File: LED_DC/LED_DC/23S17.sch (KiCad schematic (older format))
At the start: 27 parts

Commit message: Removed redundant files
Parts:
- removed C?: CP, symbol Device:CP
- removed R? (x9): 10K, symbol Device:R
- removed U?: MCP23S17_SO, Package_SO:SOIC-28W_7.5x17.9mm_P1.27mm, symbol Interface_Expansion:MCP23S17_SO
- added DS?: HY1602E, Display:HY1602E, symbol Display_Character:HY1602E
- added R10, R11, R4, R5, R6, R7, R8, R9: R, symbol Device:R
- added U1: 74HC238, symbol 74xx_IEEE:74HC238
- added U2: ULN2803A, symbol Transistor_Array:ULN2803A
- gave numbers to parts that had none: 16
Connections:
- net labels added: +5V, I1, I2, I3, I_A, I_B, I_C, I_D, I_DP, I_E, I_F, I_G
- net labels removed: MISO, MOSI, SCLK, SS
- wire segments 39 -> 56
- no-connect marks 0 -> 1
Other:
- note added: "COMM is generally used during driving Relays, for LEDs not needed"
- note added: "Digit Chose X"
- note added: "Digit Scan selection Decoder logic"
- note added: "Future Support For LCD Display."
- note added: "High Side,"
- note added: "Low Side, LED Segment Current Sink Driver"
- note added: "Segment Chose X"
- moved on the sheet: R12, R13, R14, R15, R16, R17, R18, R19

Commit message: updated the led schematic.
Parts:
- removed Q2, Q3, Q4, Q5, Q6, Q7, Q8: FDV304P, digikey-footprints:SOT-23-3, symbol dk_Transistors-FETs-MOSFETs-Single:DMG2305UX-13
- removed R12, R16: R, symbol Device:R
- removed R13, R14, R15, R17, R18, R19: 10K, symbol Device:R
- added Q? (x7): FDV304P, digikey-footprints:SOT-23-3, symbol LED_DC-rescue:DMG2305UX-13-dk_Transistors-FETs-MOSFETs-Single
- Q1: symbol dk_Transistors-FETs-MOSFETs-Single:DMG2305UX-13 -> LED_DC-rescue:DMG2305UX-13-dk_Transistors-FETs-MOSFETs-Single
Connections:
- net labels added: C1, C2, C3, D0, D1, D2, D3, D4, D5, D6, D7
- wire segments 56 -> 73
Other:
- moved on the sheet: DS?, R5

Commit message: Added keypad connector.
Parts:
- removed R10, R11, R5, R6, R7, R8, R9: R, symbol Device:R
- added R? (x7): R, symbol Device:R
- added R? (x3): R_Small, symbol Device:R_Small
- added TP?: TestPoint, symbol Connector:TestPoint
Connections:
- net labels removed: +3.3V, I1, I2, I3, I_A, I_B, I_C, I_D, I_DP, I_E, I_F, I_G, VDD
- wire segments 73 -> 74
- no-connect marks 1 -> 0
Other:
- moved on the sheet: R4

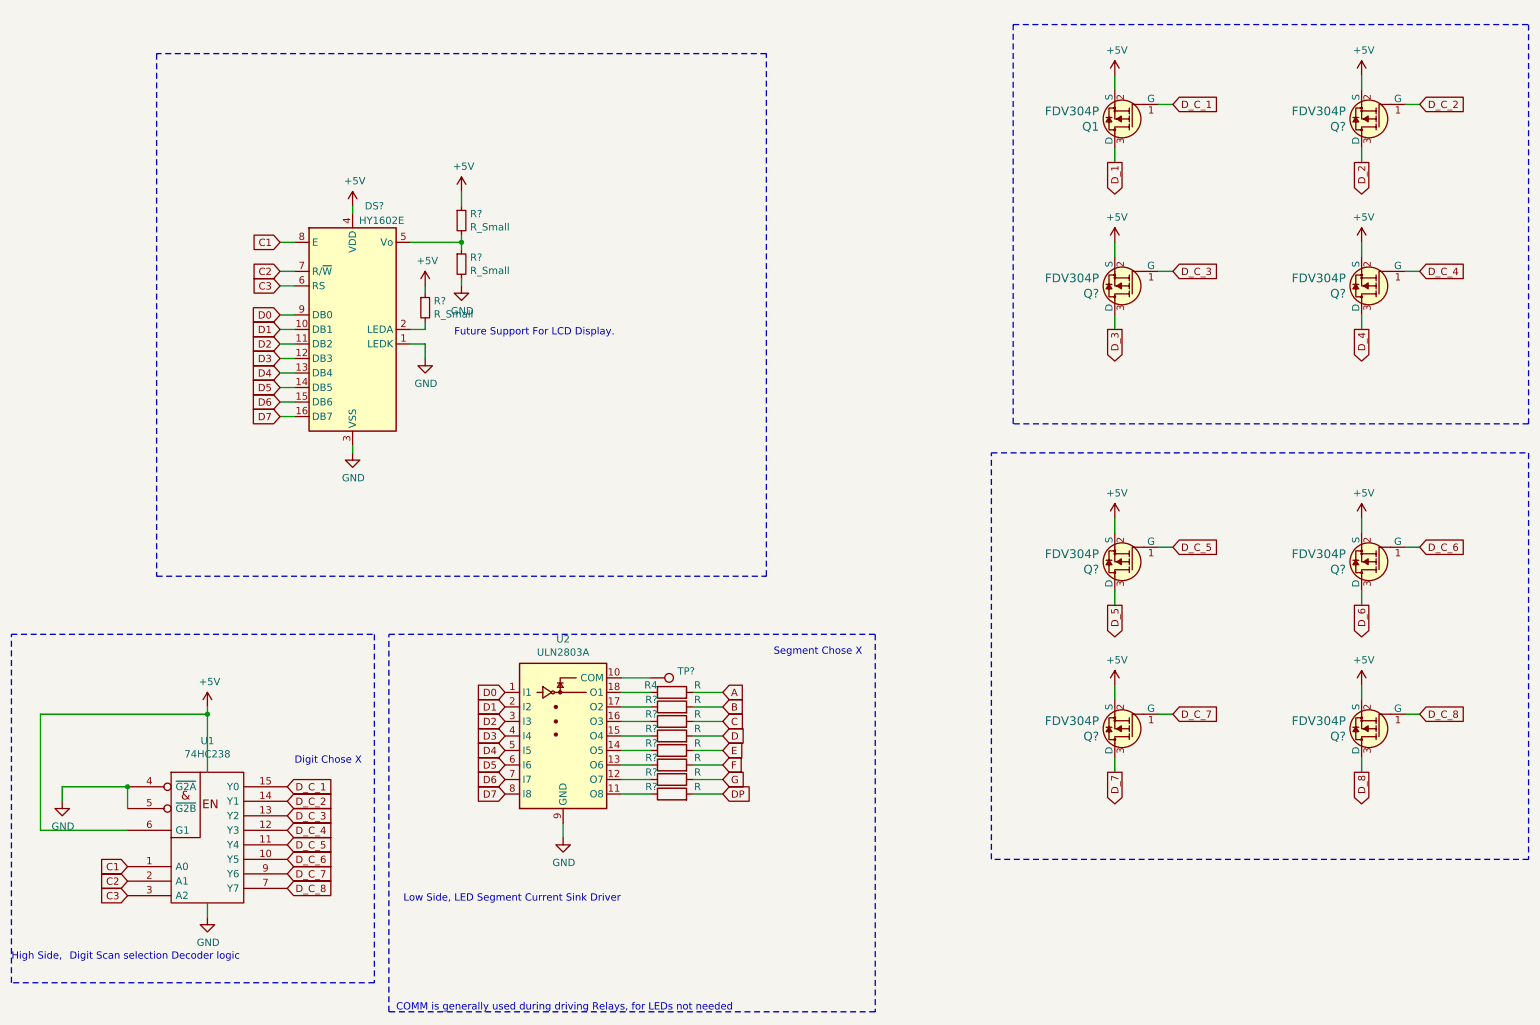
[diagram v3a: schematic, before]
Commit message: Added foot prints for the components.
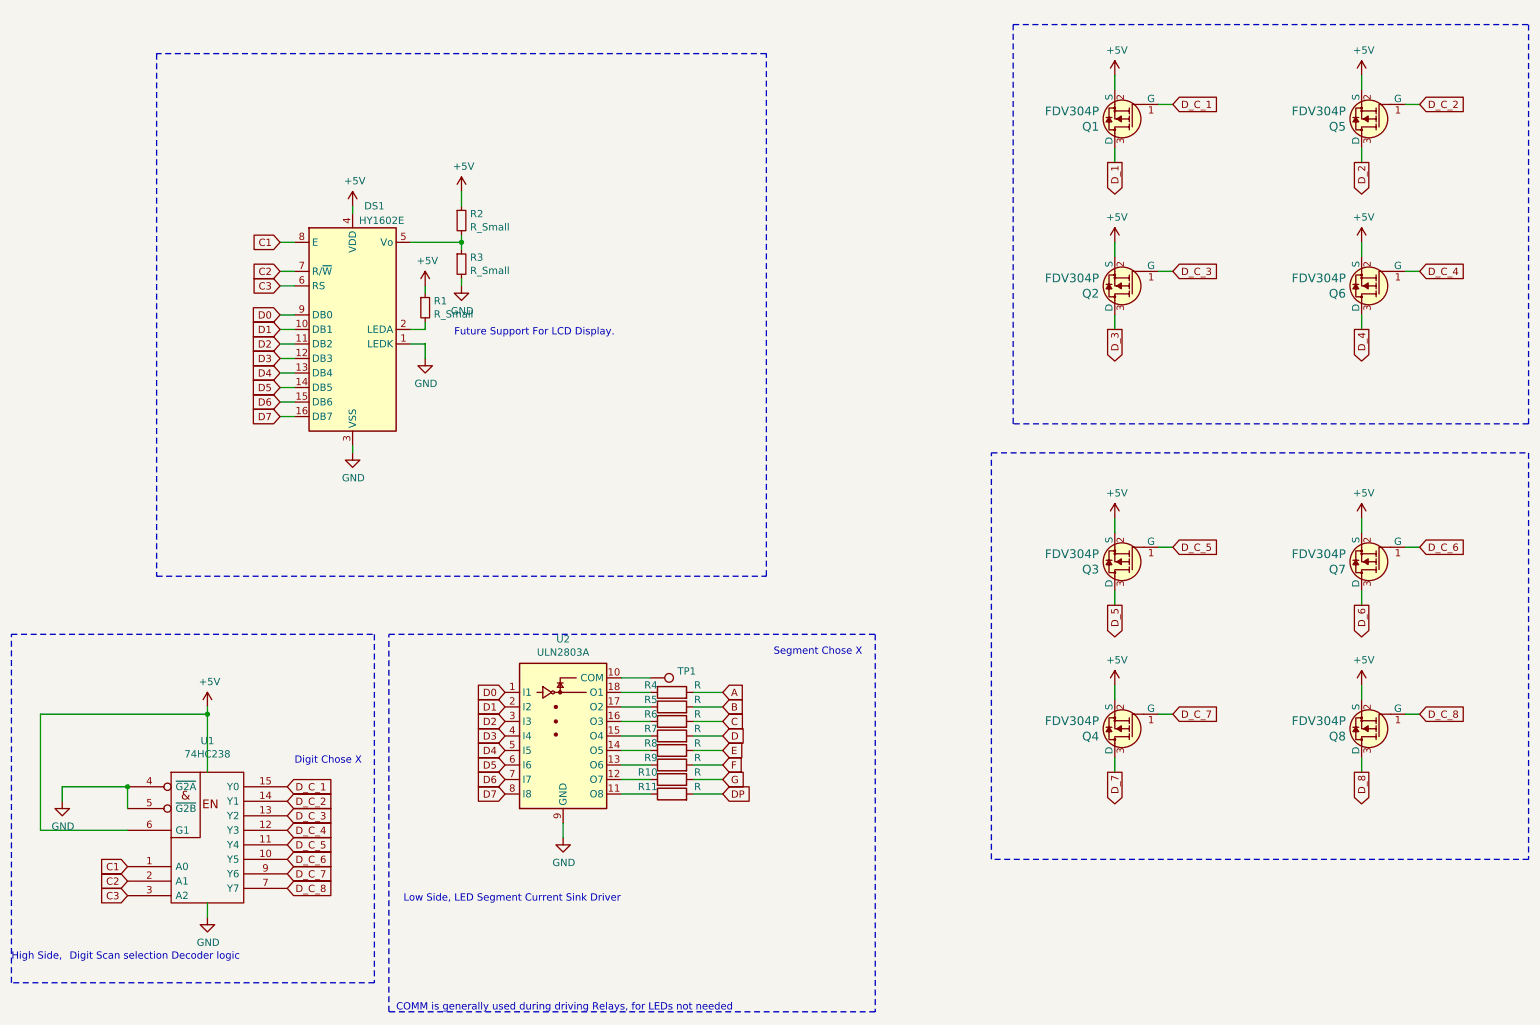
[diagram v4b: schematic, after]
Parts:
- Q1: footprint digikey-footprints:SOT-23-3 -> Package_TO_SOT_SMD:SOT-23_Handsoldering
- Q2, Q3, Q4, Q5, Q6, Q7, Q8: renamed from Q?; footprint digikey-footprints:SOT-23-3 -> Package_TO_SOT_SMD:SOT-23_Handsoldering
- R1, R10, R11, R2, R3, R5, R6, R7, R8, R9: renamed from R?; footprint (none) -> Resistor_SMD:R_0603_1608Metric
- R4: footprint (none) -> Resistor_SMD:R_0603_1608Metric
- TP1: renamed from TP?; footprint (none) -> TestPoint:TestPoint_Pad_D1.5mm
- U1: footprint (none) -> Package_SO:SO-16_3.9x9.9mm_P1.27mm
- U2: footprint (none) -> Package_SO:SOIC-18W_7.5x11.6mm_P1.27mm
- gave numbers to parts that had none: 1

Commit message: updated the PCB.
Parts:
- DS1: footprint Display:HY1602E -> Connector_PinHeader_2.54mm:PinHeader_1x16_P2.54mm_Vertical
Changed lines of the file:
@@
 F 0 "DS1" H 3000 3550 50  0000 C CNN
 F 1 "HY1602E" H 3050 3450 50  0000 C CNN
-F 2 "Display:HY1602E" H 2850 1800 50  0001 C CIN
+F 2 "Connector_PinHeader_2.54mm:PinHeader_1x16_P2.54mm_Vertical" H 2850 1800 50  0001 C CIN
 F 3 "http://www.icbank.com/data/ICBShop/board/HY1602E.pdf" H 3050 2800 50  0001 C CNN
 	1    2850 2700

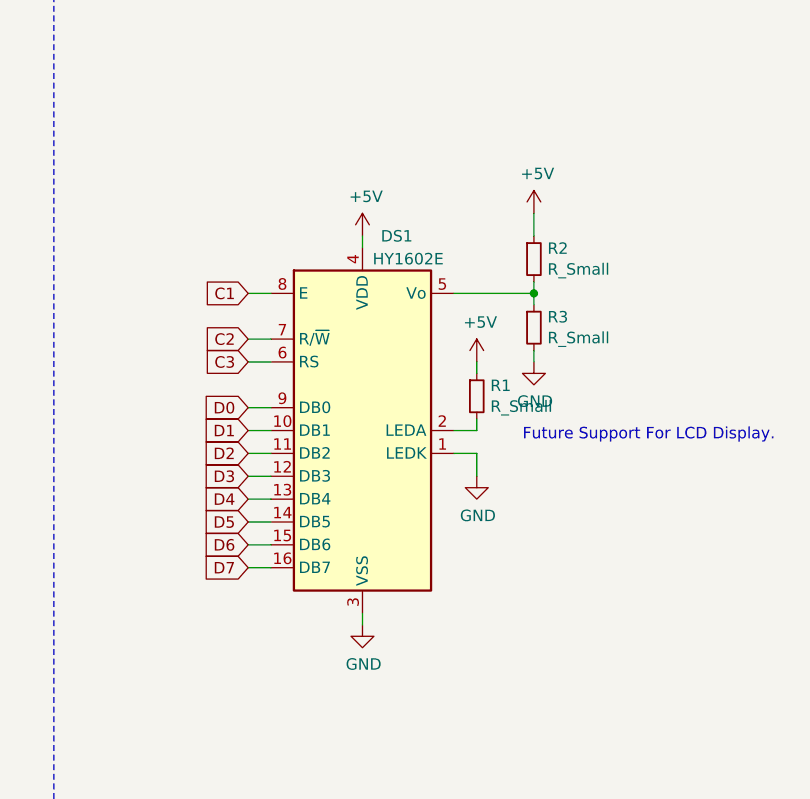
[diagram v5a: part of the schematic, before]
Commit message: updated the schematic after feedback.
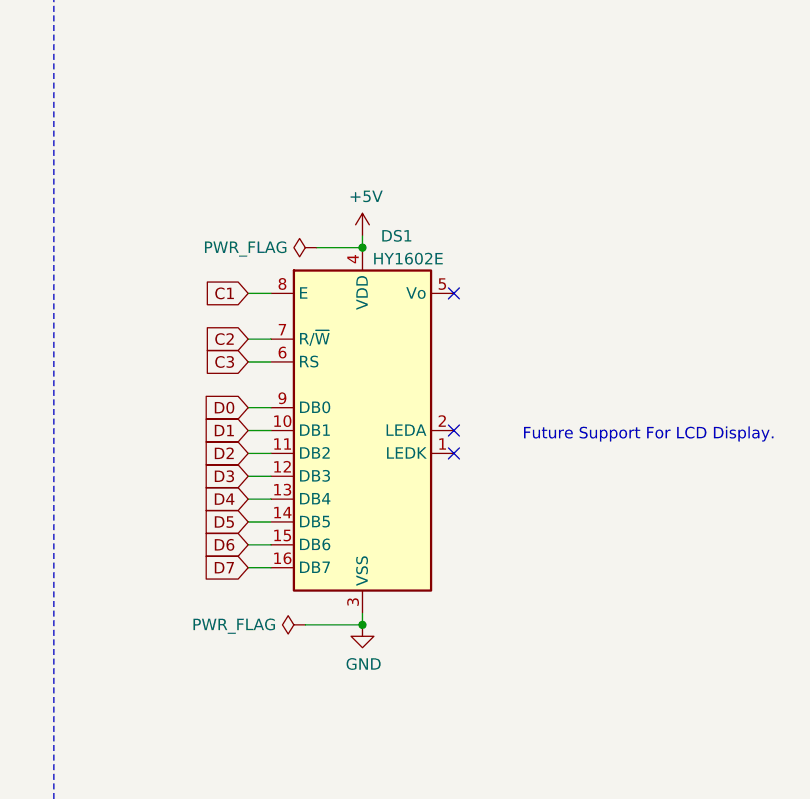
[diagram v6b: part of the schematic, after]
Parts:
- removed R1, R2, R3: R_Small, Resistor_SMD:R_0603_1608Metric, symbol Device:R_Small
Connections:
- net GND: no longer DS1.1 (LEDK)
- no-connect marks 0 -> 3
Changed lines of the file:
@@
 COMM is generally used during driving Relays, for LEDs not needed
-$Comp
-L Display_Character:HY1602E DS1
-U 1 1 5FC030D8
-P 2850 2700
-F 0 "DS1" H 3000 3550 50  0000 C CNN
-F 1 "HY1602E" H 3050 3450 50  0000 C CNN
-F 2 "Connector_PinHeader_2.54mm:PinHeader_1x16_P2.54mm_Vertical" H 2850 1800 50  0001 C CIN
-F 3 "http://www.icbank.com/data/ICBShop/board/HY1602E.pdf" H 3050 2800 50  0001 C CNN
-	1    2850 2700
-	1    0    0    -1
-$EndComp
 $Comp
 L power:+5V #PWR05
@@
 Wire Notes Line
 	5700 800  1500 800
-Text Notes 3550 2750 0    50   ~ 0
-Future Support For LCD Display.
 Wire Wire Line
 	2850 3500 2850 3550
@@
 	4900 5100 4700 5100
 $Comp
-L power:GND #PWR010
-U 1 1 5FEAB2F7
-P 3350 2900
-F 0 "#PWR010" H 3350 2650 50  0001 C CNN
-F 1 "GND" H 3355 2727 50  0000 C CNN
-F 2 "" H 3350 2900 50  0001 C CNN
-F 3 "" H 3350 2900 50  0001 C CNN
-	1    3350 2900
-	1    0    0    -1
-$EndComp
-$Comp
-L power:+5V #PWR09
-U 1 1 5FEAB829
-P 3350 2400
-F 0 "#PWR09" H 3350 2250 50  0001 C CNN
-F 1 "+5V" H 3365 2573 50  0000 C CNN
-F 2 "" H 3350 2400 50  0001 C CNN
-F 3 "" H 3350 2400 50  0001 C CNN
-	1    3350 2400
-	1    0    0    -1
-$EndComp
-$Comp
-L Device:R_Small R1
-U 1 1 5FEAC3CE
-P 3350 2550
-F 0 "R1" H 3409 2596 50  0000 L CNN
-F 1 "R_Small" H 3409 2505 50  0000 L CNN
-F 2 "Resistor_SMD:R_0603_1608Metric" H 3350 2550 50  0001 C CNN
-F 3 "~" H 3350 2550 50  0001 C CNN
-	1    3350 2550
-	1    0    0    -1
-$EndComp
-Wire Wire Line
-	3350 2650 3350 2700
-Wire Wire Line
-	3350 2700 3250 2700
-Wire Wire Line
-	3250 2800 3350 2800
-Wire Wire Line
-	3350 2800 3350 2900
-Wire Wire Line
-	3350 2450 3350 2400
-$Comp
-L Device:R_Small R2
-U 1 1 5FEB1440
-P 3600 1950
-F 0 "R2" H 3659 1996 50  0000 L CNN
-F 1 "R_Small" H 3659 1905 50  0000 L CNN
-F 2 "Resistor_SMD:R_0603_1608Metric" H 3600 1950 50  0001 C CNN
-F 3 "~" H 3600 1950 50  0001 C CNN
-	1    3600 1950
-	1    0    0    -1
-$EndComp
-$Comp
-L Device:R_Small R3
-U 1 1 5FEB1C82
-P 3600 2250
-F 0 "R3" H 3659 2296 50  0000 L CNN
-F 1 "R_Small" H 3659 2205 50  0000 L CNN
-F 2 "Resistor_SMD:R_0603_1608Metric" H 3600 2250 50  0001 C CNN
-F 3 "~" H 3600 2250 50  0001 C CNN
-	1    3600 2250
-	1    0    0    -1
-$EndComp
-$Comp
-L power:GND #PWR014
-U 1 1 5FEB1F5D
-P 3600 2400
-F 0 "#PWR014" H 3600 2150 50  0001 C CNN
-F 1 "GND" H 3605 2227 50  0000 C CNN
-F 2 "" H 3600 2400 50  0001 C CNN
-F 3 "" H 3600 2400 50  0001 C CNN
-	1    3600 2400
-	1    0    0    -1
-$EndComp
-$Comp
-L power:+5V #PWR013
-U 1 1 5FEB20FA
-P 3600 1750
-F 0 "#PWR013" H 3600 1600 50  0001 C CNN
-F 1 "+5V" H 3615 1923 50  0000 C CNN
-F 2 "" H 3600 1750 50  0001 C CNN
-F 3 "" H 3600 1750 50  0001 C CNN
-	1    3600 1750
-	1    0    0    -1
-$EndComp
-Wire Wire Line
-	3600 1750 3600 1850
-Wire Wire Line
-	3600 2050 3600 2100
-Wire Wire Line
-	3600 2350 3600 2400
-Wire Wire Line
-	3250 2100 3600 2100
-Connection ~ 3600 2100
-Wire Wire Line
-	3600 2100 3600 2150
+L Display_Character:HY1602E DS1
+U 1 1 5FC030D8
+P 2850 2700
+F 0 "DS1" H 3000 3550 50  0000 C CNN
+F 1 "HY1602E" H 3050 3450 50  0000 C CNN
+F 2 "Connector_PinHeader_2.54mm:PinHeader_1x16_P2.54mm_Vertical" H 2850 1800 50  0001 C CIN
+F 3 "http://www.icbank.com/data/ICBShop/board/HY1602E.pdf" H 3050 2800 50  0001 C CNN
+	1    2850 2700
+	1    0    0    -1
+$EndComp
+Text Notes 3550 2750 0    50   ~ 0
+Future Support For LCD Display.
+NoConn ~ 3250 2100
+NoConn ~ 3250 2700
+NoConn ~ 3250 2800
+$Comp
+L power:PWR_FLAG #FLG0101
+U 1 1 60176418
+P 2650 1900
+F 0 "#FLG0101" H 2650 1975 50  0001 C CNN
+F 1 "PWR_FLAG" V 2650 2027 50  0000 L CNN
+F 2 "" H 2650 1900 50  0001 C CNN
+F 3 "~" H 2650 1900 50  0001 C CNN
+	1    2650 1900
+	0    -1   -1   0
+$EndComp
+$Comp
+L power:PWR_FLAG #FLG0102
+U 1 1 60176CCD
+P 2600 3550
+F 0 "#FLG0102" H 2600 3625 50  0001 C CNN
+F 1 "PWR_FLAG" V 2600 3677 50  0000 L CNN
+F 2 "" H 2600 3550 50  0001 C CNN
+F 3 "~" H 2600 3550 50  0001 C CNN
+	1    2600 3550
+	0    -1   -1   0
+$EndComp
+Wire Wire Line
+	2600 3550 2850 3550
+Connection ~ 2850 3550
+Wire Wire Line
+	2650 1900 2850 1900
+Connection ~ 2850 1900
 $EndSCHEMATC

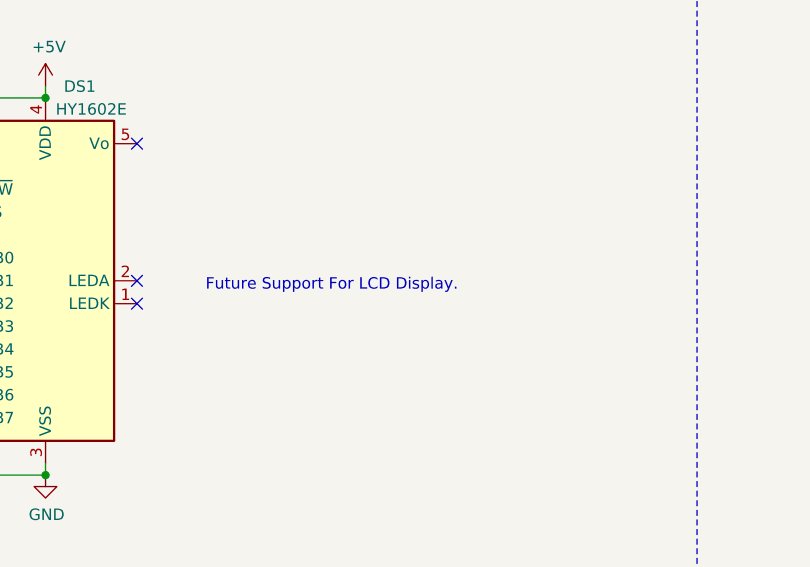
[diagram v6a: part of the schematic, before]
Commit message: Added text to the schematic sections.
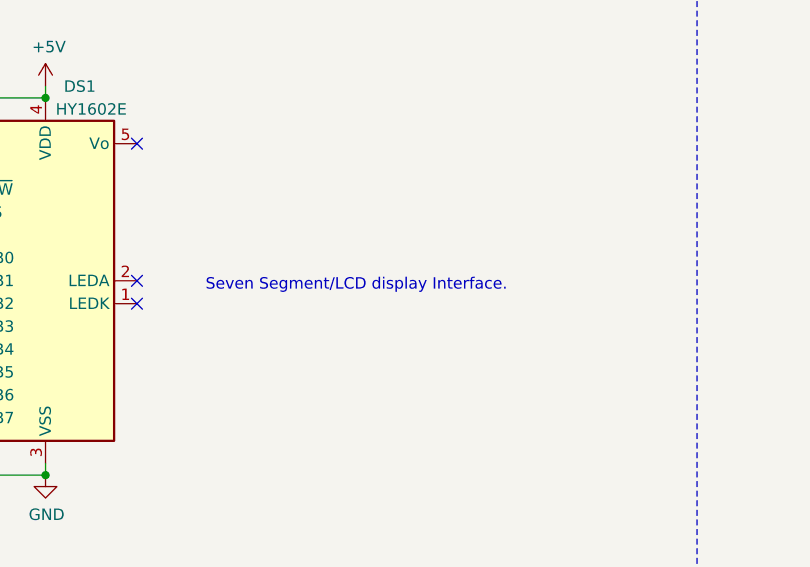
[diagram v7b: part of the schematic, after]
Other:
- note added: "Seven Segment/LCD display Interface."
- note removed: "Future Support For LCD Display."
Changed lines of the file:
@@
 $EndComp
 Text Notes 3550 2750 0    50   ~ 0
-Future Support For LCD Display.
+Seven Segment/LCD display Interface.
 NoConn ~ 3250 2100
 NoConn ~ 3250 2700

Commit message: Updated the schematic.
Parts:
- DS1: value HY1602E -> RC1602A; symbol Display_Character:HY1602E -> Display_Character:RC1602A
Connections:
- net +5V: now also DS1.2 (VDD); no longer DS1.4 (VDD)
- net C1: now also DS1.4 (RS); no longer DS1.8 (E)
- net C2: now also DS1.5 (R/W); no longer DS1.7 (R/~W)
- net D0: now also DS1.7 (DB0); no longer DS1.9 (DB0)
- net D1: now also DS1.8 (DB1); no longer DS1.10 (DB1)
- net D2: now also DS1.9 (DB2); no longer DS1.11 (DB2)
- net D3: now also DS1.10 (DB3); no longer DS1.12 (DB3)
- net D4: now also DS1.11 (DB4); no longer DS1.13 (DB4)
- net D5: now also DS1.12 (DB5); no longer DS1.14 (DB5)
- net D6: now also DS1.13 (DB6); no longer DS1.15 (DB6)
- net D7: now also DS1.14 (DB7); no longer DS1.16 (DB7)
- net GND: now also DS1.1 (VSS); no longer DS1.3 (VSS)
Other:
- moved on the sheet: DS1
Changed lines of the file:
@@
 Wire Wire Line
 	9800 5750 9800 5650
-Text GLabel 2350 2100 0    50   Input ~ 0
+Text GLabel 2350 2300 0    50   Input ~ 0
 C1
-Text GLabel 2350 2300 0    50   Input ~ 0
+Text GLabel 2350 2400 0    50   Input ~ 0
 C2
-Text GLabel 2350 2400 0    50   Input ~ 0
+Text GLabel 2350 2500 0    50   Input ~ 0
 C3
 Text GLabel 2350 2600 0    50   Input ~ 0
@@
 D7
 Wire Wire Line
-	2350 2100 2450 2100
-Wire Wire Line
-	2450 2300 2350 2300
-Wire Wire Line
-	2350 2400 2450 2400
-Wire Wire Line
 	2450 2600 2350 2600
 Wire Wire Line
@@
 	4900 5100 4700 5100
 $Comp
-L Display_Character:HY1602E DS1
+L Display_Character:RC1602A DS1
 U 1 1 5FC030D8
-P 2850 2700
-F 0 "DS1" H 3000 3550 50  0000 C CNN
-F 1 "HY1602E" H 3050 3450 50  0000 C CNN
-F 2 "Connector_PinHeader_2.54mm:PinHeader_1x16_P2.54mm_Vertical" H 2850 1800 50  0001 C CIN
-F 3 "http://www.icbank.com/data/ICBShop/board/HY1602E.pdf" H 3050 2800 50  0001 C CNN
-	1    2850 2700
+P 2850 2800
+F 0 "DS1" H 3000 3650 50  0000 C CNN
+F 1 "RC1602A" H 3050 3550 50  0000 C CNN
+F 2 "Connector_PinHeader_2.54mm:PinHeader_1x16_P2.54mm_Vertical" H 2850 1900 50  0001 C CIN
+F 3 "http://www.icbank.com/data/ICBShop/board/HY1602E.pdf" H 3050 2900 50  0001 C CNN
+	1    2850 2800
 	1    0    0    -1
 $EndComp
 Text Notes 3550 2750 0    50   ~ 0
 Seven Segment/LCD display Interface.
-NoConn ~ 3250 2100
-NoConn ~ 3250 2700
-NoConn ~ 3250 2800
 $Comp
 L power:PWR_FLAG #FLG0101
@@
 	2650 1900 2850 1900
 Connection ~ 2850 1900
+Wire Wire Line
+	2850 1900 2850 2100
+NoConn ~ 3250 2600
+NoConn ~ 3250 3000
+NoConn ~ 3250 3100
+Wire Wire Line
+	2350 2300 2450 2300
+Wire Wire Line
+	2450 2400 2350 2400
+Wire Wire Line
+	2350 2500 2450 2500
 $EndSCHEMATC
